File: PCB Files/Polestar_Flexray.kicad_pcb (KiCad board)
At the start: 4 copper layers, 82 x 43 mm, 66 parts, among them J1 JAE DX07S024XJ1R1100, J2 Molex 2125280400, J3 JAE MX34032NF4, J4 JAE MX34032NF4, K1 G5V-2-H1 DC12, K2 G5V-2-H1 DC12, K3 G5V-2-H1 DC12, Q1 DMN3200U-7, Q2 DMN3200U-7, U1 Vishay DG419LEDY-T1-GE4, U2 Vishay DG419LEDY-T1-GE4, U3 LM53600-Q1, U4 XIAO_RP2350, U5 TJA1082, U6 TJA1082, U8 TCAN4550-Q1, Y1 40MHz

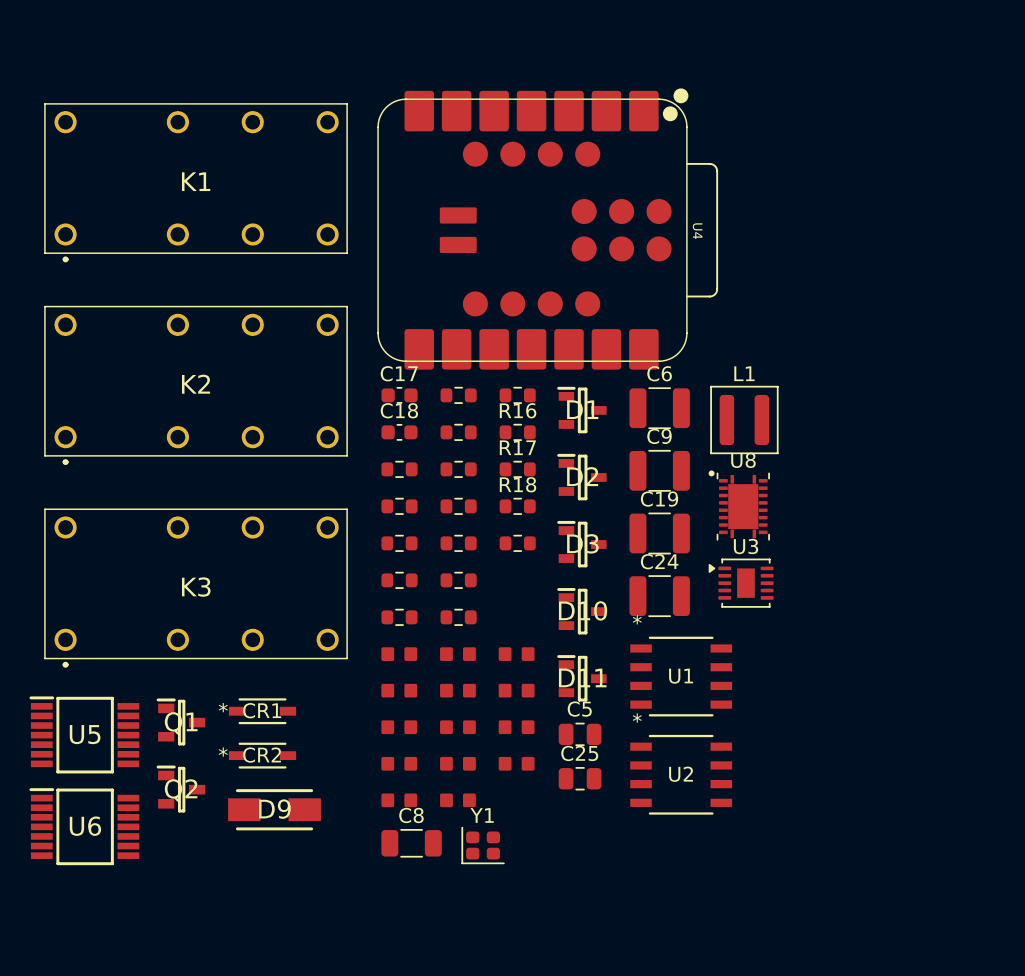
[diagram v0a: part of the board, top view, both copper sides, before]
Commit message: Add input protection, fix TJA1082 mode strap and Q3 pad mapping
Protection and supply hardening on the only power input, plus three
silent faults found by review.

Input (J2 is the sole feed and sits on constant battery):
- F1 Walter Elec 1206T3A63V, 3A 63V time-lag (LCSC C354897). Previously
  there was no fuse anywhere in the design.
- Q3 reverse-polarity P-FET (DMP4015SSS-13), drain on the fused battery,
  source on VIN, with D14 16V gate clamp and R20 100k pulldown. D9 moved
  to the load side of Q3; as a uni-directional TVS it was forward-biasing
  on a reversed input, and CR1 with it, putting two SMD diodes straight
  across the battery.
- D14 is 16V so it stays off at 14.4V, costing zero standby current.

Q3 pad mapping (would have shipped broken):
- Q3 used a 3-pin generic FET symbol on an 8-pad SOIC-8. KiCad matches pin
  numbers to pad numbers, so gate/drain/source landed on pads 1-3 - all
  three of which are Source on the DMP4015SSS. VBAT_F was shorted to VIN
  through the package and the real gate and drain floated. The board would
  have powered up normally with no reverse protection at all, and ERC does
  not check pad mapping. Fixed with My_Components:DMP4015SSS-13, an 8-pin
  symbol with S on 1-3, G on 4, D on 5-8.

TJA1082 error indication (U5, U6):
- SCSN tied high did not disable SPI. Per datasheet rev 6 sec 6.8 the part
  powers up in SPI mode, where error flags latch until a full 16-bit status
  readout. VIO comes from the XIAO LDO so it rises after VCC, setting UVVIO
  on every power-up, and with SCLK/SDO unconnected nothing could ever clear
  it - ERRN would have latched low forever. Now strapped to simple error
  indication mode: SCSN to GND, SCLK to +3V3.

XIAO supply:
- D12 Schottky + C26 10uF isolating the XIAO 5V pad, which is raw USB VBUS.
  Plugging in USB to flash it previously fought the buck (forced PWM allows
  reverse current) or back-fed VIN through the buck body diode.

DG419 supply and comma-side termination:
- V+ now fed via D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
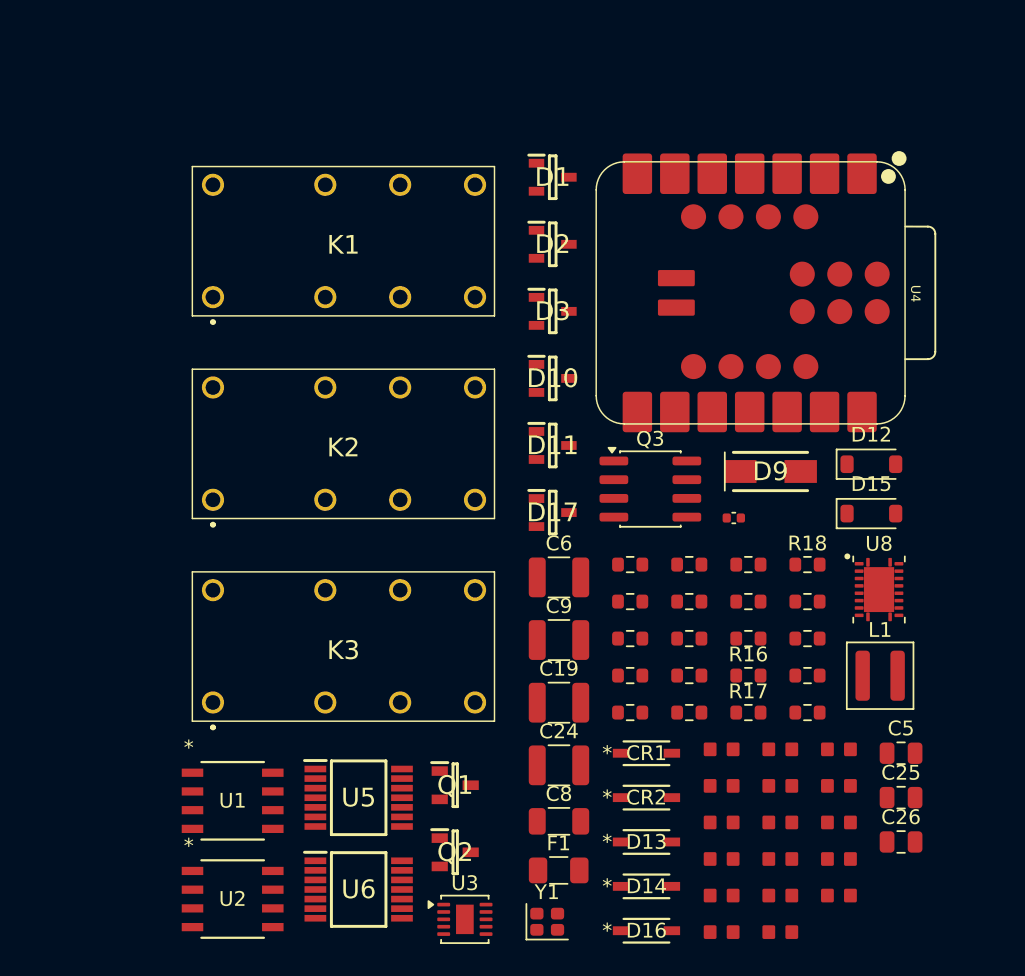
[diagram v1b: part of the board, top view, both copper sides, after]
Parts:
- added C26: 10uF, Footprints:SAMS CL21B106KAYQNNE, F.Cu at (145.1, 179.4)
- added C27: 10nF, Footprints:SAMS CL05B103KA5NNNC, F.Cu at (133.8, 157.4)
- added C28: 100nF, Footprints:SAMS CL10B104KB8NNNC, F.Cu at (140.9, 183.0)
- added D12: DSK14, Footprints:SCHOTTKY - 1A, F.Cu at (143.1, 153.7)
- added D13: BZT52C5V1, Footprints:SOD123_DIO, F.Cu at (127.9, 179.4)
- added D14: BZT52C16, Footprints:SOD123_DIO, F.Cu at (127.9, 182.4)
- added D15: DSK14, Footprints:SCHOTTKY - 1A, F.Cu at (143.1, 157.1)
- added D16: BZT52C12, Footprints:SOD123_DIO, F.Cu at (127.9, 185.4)
- added D17: PESD1CAN, Footprints:PESD1CAN, F.Cu at (121.5, 157.0)
- added F1: 3A, Footprints:Walter Elec 1206T3A63V, F.Cu at (121.9, 181.3)
- added Q3: DMP4015SSS-13, Package_SO:SOIC-8_3.9x4.9mm_P1.27mm, F.Cu at (128.1, 155.4)
- added R20: 100K, Footprints:Rohm ESR03EZPJ104, F.Cu at (138.8, 165.6)
- added R21: 3.3K, Footprints:Rohm ESR03EZPJ332, F.Cu at (138.8, 168.1)
- added R22: 120, Footprints:Rohm ESR03EZPJ121, F.Cu at (138.8, 170.6)
- C17, C18: value 2.2pF -> 2.2pF C0G; footprint Capacitor_SMD:C_0603_1608Metric -> Footprints:FH 0603CG2R2C500NT
- R16: value 60R4 -> 0R; footprint Footprints:YAGEO AC0603FR-7W60R4L -> Footprints:R_0603_1608Metric
- R6: value 1K -> 10K; footprint Footprints:Rohm ESR03EZPJ102 -> Footprints:Rohm ESR03EZPJ103
- R8: value 1K -> 3.3K; footprint Footprints:Rohm ESR03EZPJ102 -> Footprints:Rohm ESR03EZPJ332
- U3: value LM53600-Q1 -> LM53600LQDSXRQ1
- Y1: value 40MHz -> 40MHz NX2016SA
- moved C17 42.7 mm to (136.9, 183.0)
- moved C18 42.6 mm to (136.9, 185.5)
- moved D9 40.7 mm to (136.3, 154.2)
- moved U1 31.6 mm to (99.8, 176.6)
- moved U2 31.6 mm to (99.8, 183.2)
- moved U3 29.7 mm to (115.5, 184.6)
- moved CR1 26.2 mm to (127.9, 173.4)
- moved CR2 26.2 mm to (127.9, 176.4)
- moved C10 26.0 mm to (133.0, 185.5)
- moved C1 22.8 mm to (133.0, 173.1)
- moved C3 22.8 mm to (133.0, 178.1)
- moved C4 22.8 mm to (133.0, 180.5)
- moved C2 22.8 mm to (133.0, 175.6)
- moved C7 22.8 mm to (133.0, 183.0)
- moved C20 22.8 mm to (140.9, 173.1)
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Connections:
- net Net-(Q1-G) renamed /IGN_GATE
- J2 pad 4: VIN -> /VBAT
- U1 pad 4: VIN -> /SW_VCC
- U1 pad 5: VIN -> +5V
- U2 pad 4: VIN -> /SW_VCC
- U2 pad 5: VIN -> +5V
- U2 pad 8: unconnected-(U2-NO-Pad8) -> Net-(U2-NO)
- U4 pad 14: +5V -> /+5V_XIAO
- U5 pad 7: unconnected-(U5-SCLK-Pad7) -> +3V3
- U5 pad 9: +3V3 -> GND
- U6 pad 7: unconnected-(U6-SCLK-Pad7) -> +3V3
- U6 pad 9: +3V3 -> GND
